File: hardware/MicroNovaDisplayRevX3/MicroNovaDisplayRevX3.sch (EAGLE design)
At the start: 34 parts, among them Q1 BSS84, Q2 BSS84, Q3 BSS84, Q4 BSS84, Q5 BSS84, Q6 BSS84, Q7 BSS84, U1 MICRONOVA_DYSR00P401101, U2 MAX6957ATL

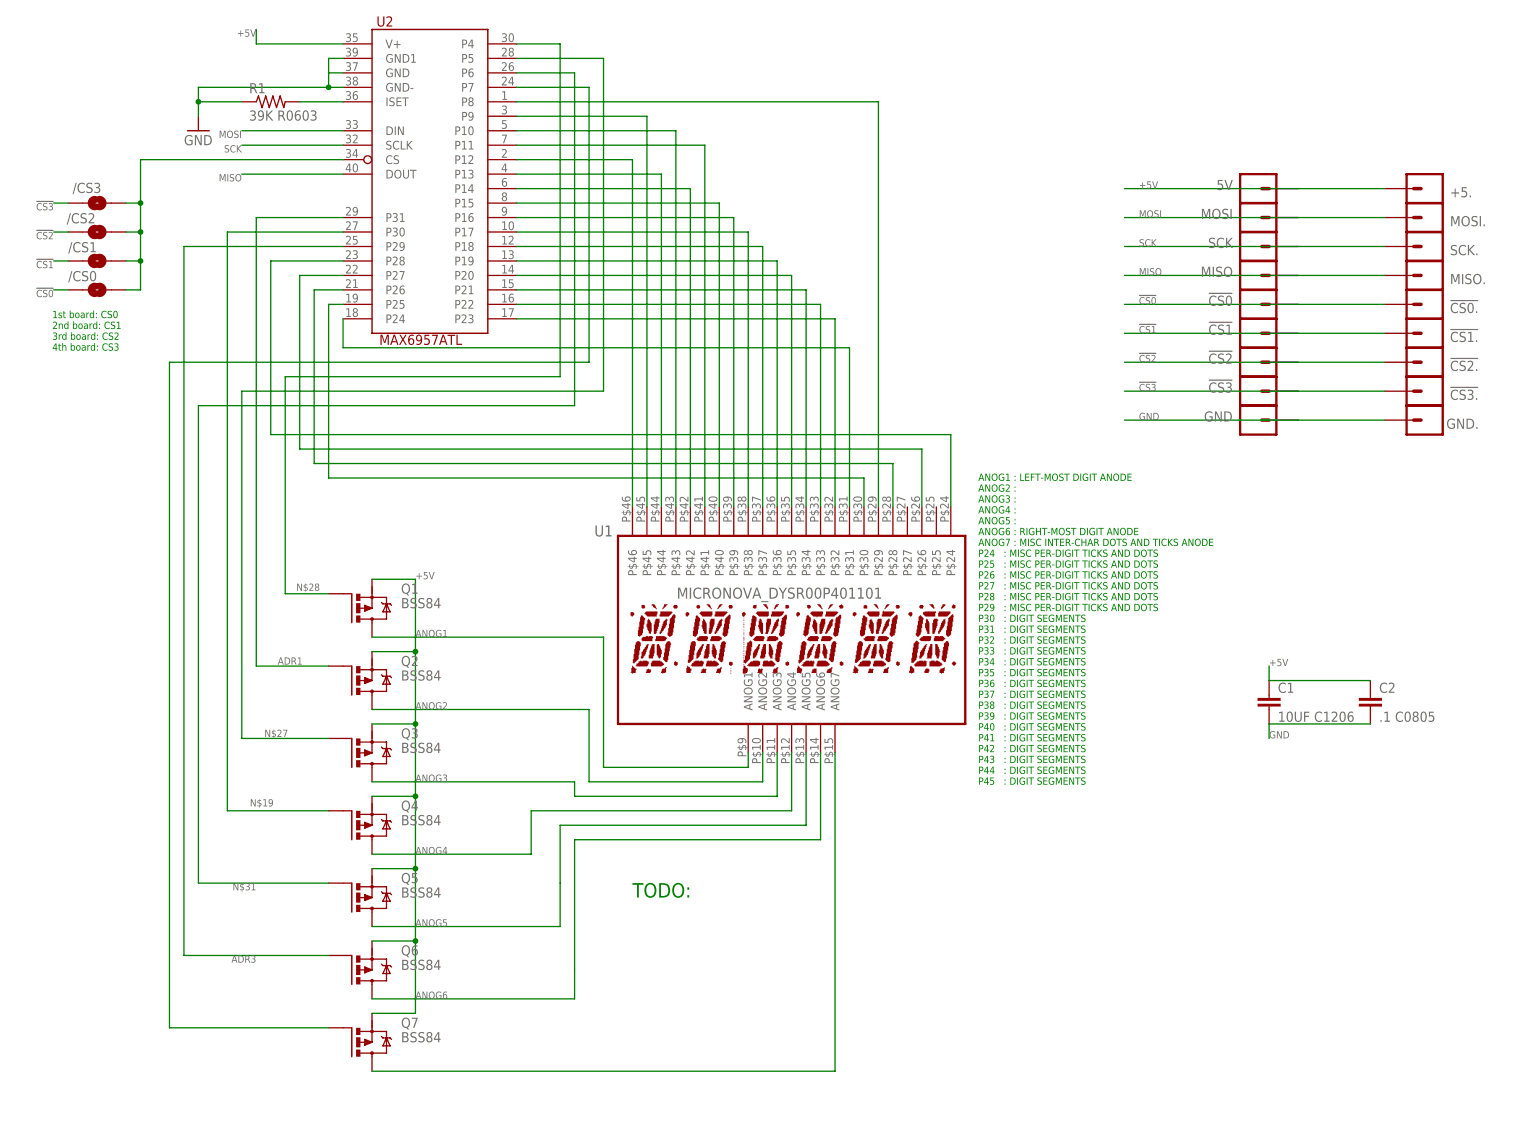
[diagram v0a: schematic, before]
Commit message: Touched up:
  hardware/MicroNovaDisplayRevX3/MicroNovaDisplayRevX3.sch

Added pdfs

  hardware/MicroNovaDisplayRevX3/MicroNovaDisplayRevX3_bot.pdf
  hardware/MicroNovaDisplayRevX3/MicroNovaDisplayRevX3_sch.pdf
  hardware/MicroNovaDisplayRevX3/MicroNovaDisplayRevX3_top.pdf
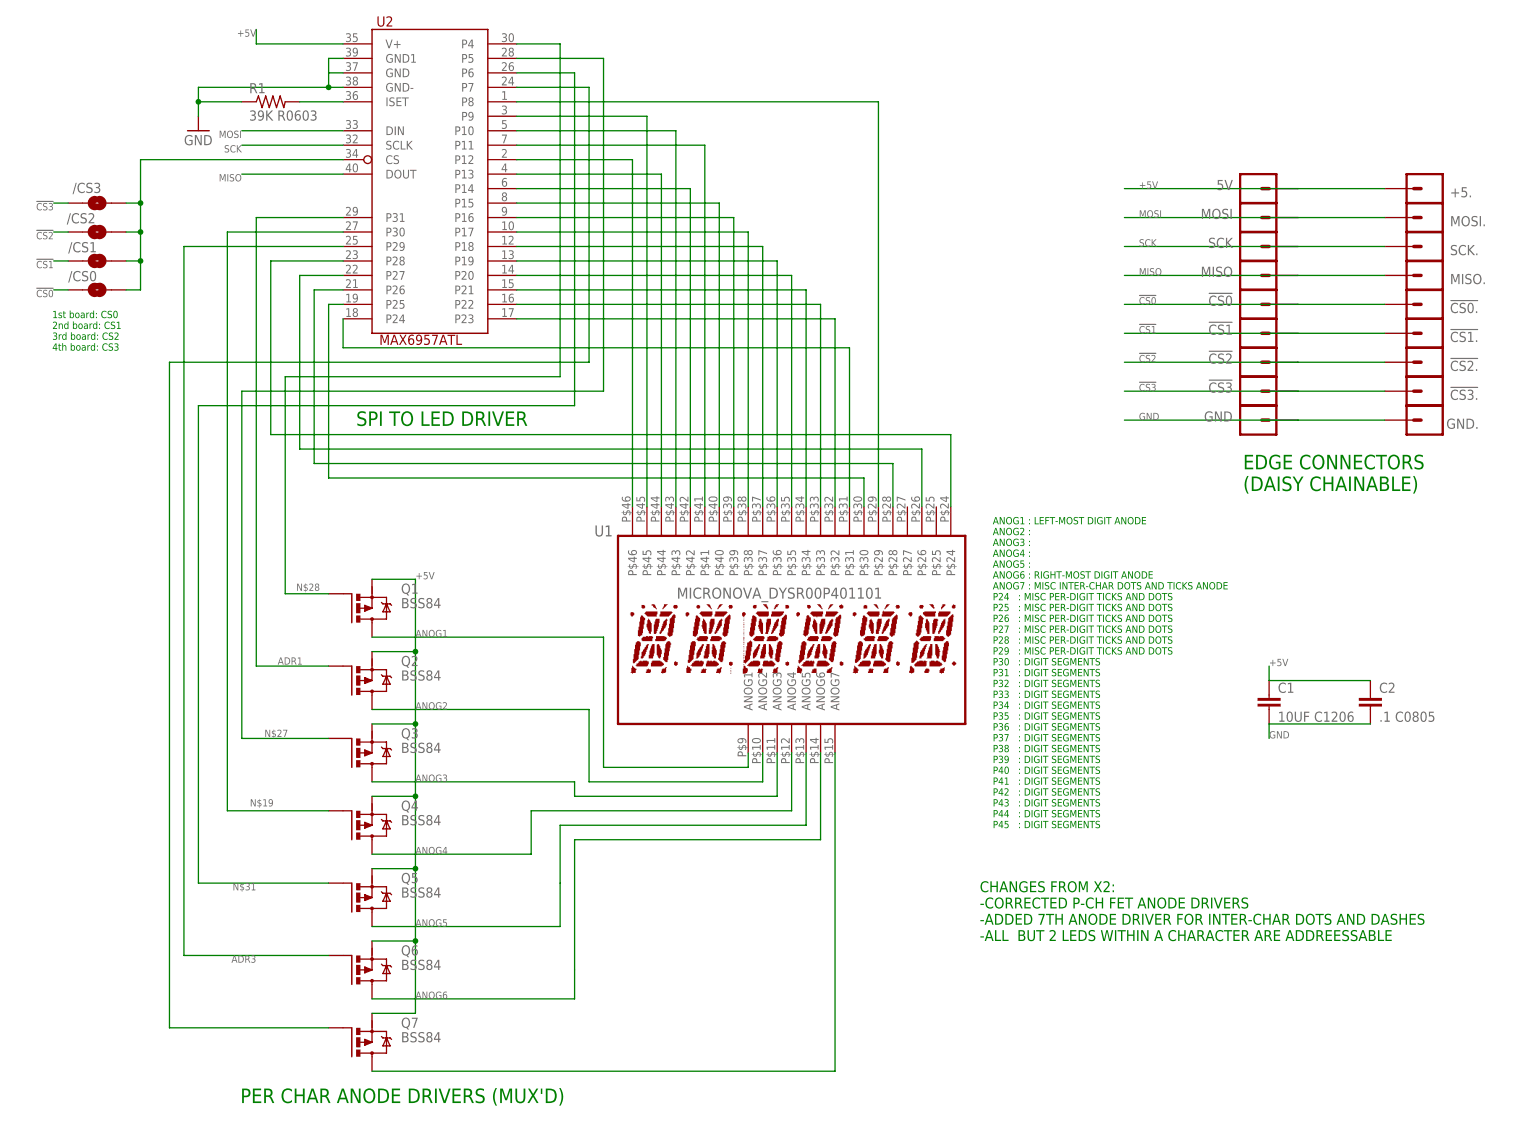
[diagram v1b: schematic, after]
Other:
- note added: "CHANGES FROM X2: -CORRECTED P-CH FET ANODE DRIVERS -ADDED 7TH ANODE DRIVER FOR INTER-CHAR DOTS AND DASHES -ALL BUT 2 LEDS WITHIN A CHARACTER ARE ADDREESSABLE"
- note added: "EDGE CONNECTORS (DAISY CHAINABLE)"
- note added: "PER CHAR ANODE DRIVERS (MUX'D)"
- note added: "SPI TO LED DRIVER"
- note removed: "TODO:"
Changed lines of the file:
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@@
 <sheet>
 <plain>
-<text x="210.566" y="35.052" size="1.27" layer="91" font="fixed" ratio="10">
+<text x="213.106" y="27.432" size="1.27" layer="91" font="fixed" ratio="10">
 ANOG1 : LEFT-MOST DIGIT ANODE
 ANOG2 :
@@
 3rd board: CS2
 4th board: CS3</text>
-<text x="149.86" y="15.24" size="2.54" layer="91">TODO:</text>
+<text x="210.82" y="7.62" size="1.905" layer="91">CHANGES FROM X2:
+-CORRECTED P-CH FET ANODE DRIVERS
+-ADDED 7TH ANODE DRIVER FOR INTER-CHAR DOTS AND DASHES
+-ALL  BUT 2 LEDS WITHIN A CHARACTER ARE ADDREESSABLE</text>
+<text x="81.026" y="-20.828" size="2.54" layer="91" font="fixed" ratio="10">PER CHAR ANODE DRIVERS (MUX'D)</text>
+<text x="101.346" y="98.044" size="2.54" layer="91" font="fixed" ratio="10">SPI TO LED DRIVER</text>
+<text x="257.048" y="86.614" size="2.54" layer="91" font="fixed" ratio="10">EDGE CONNECTORS
+(DAISY CHAINABLE)</text>
 </plain>
 <instances>
-<instance part="FRAME1" gate="G$2" x="213.36" y="17.78"/>
+<instance part="FRAME1" gate="G$2" x="213.36" y="-15.24"/>
 <instance part="GND10" gate="1" x="73.66" y="149.86"/>
 <instance part="U2" gate="G$1" x="114.3" y="142.24" smashed="yes">
